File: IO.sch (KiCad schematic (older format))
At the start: 8 parts

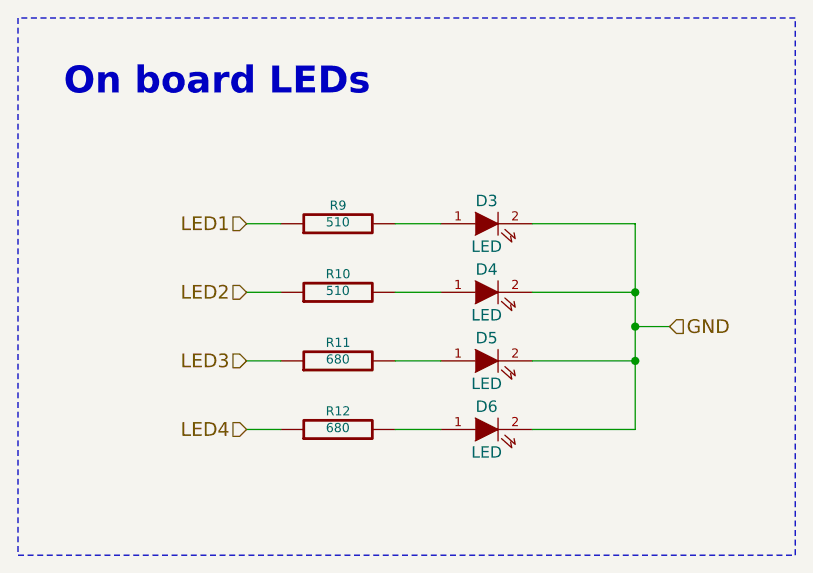
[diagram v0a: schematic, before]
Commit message: - #4 Added UART and CAN interface transceivers - Improved schematic structure - Removed all gerber outputs - Generated schematics outputs for PCB design - Updated local libraries
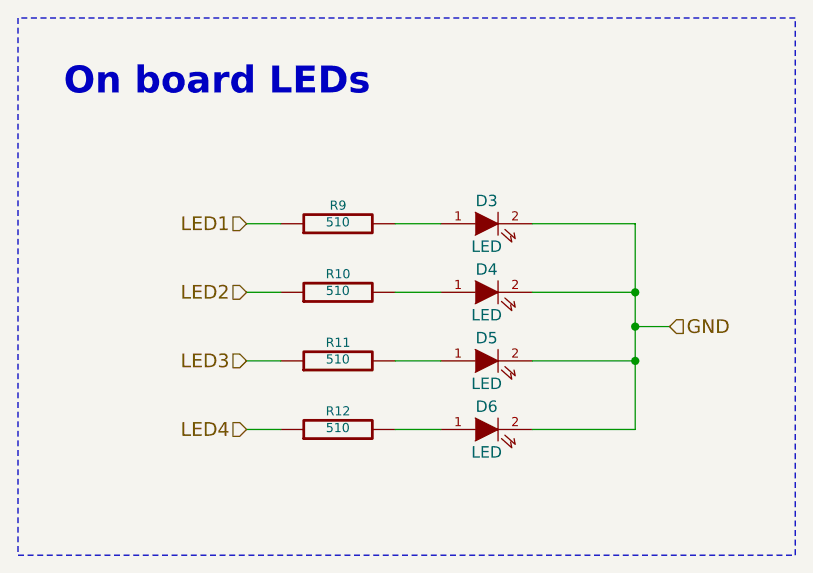
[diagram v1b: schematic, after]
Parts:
- D3, D4, D5, D6: footprint ~ -> LEDs:LED-0805
- R10, R9: footprint ~ -> Resistors_SMD:R_0603_HandSoldering
- R11, R12: value 680 -> 510; footprint ~ -> Resistors_SMD:R_0603_HandSoldering
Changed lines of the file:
@@
 F 0 "D3" H 6300 4150 50  0000 C CNN
 F 1 "LED" H 6300 3950 50  0000 C CNN
-F 2 "~" H 6300 4050 60  0000 C CNN
+F 2 "LEDs:LED-0805" H 6300 4050 60  0001 C CNN
 F 3 "~" H 6300 4050 60  0000 C CNN
 	1    6300 4050
@@
 F 0 "R9" V 5730 4050 40  0000 C CNN
 F 1 "510" V 5657 4051 40  0000 C CNN
-F 2 "~" V 5580 4050 30  0000 C CNN
+F 2 "Resistors_SMD:R_0603_HandSoldering" V 5580 4050 30  0001 C CNN
 F 3 "~" H 5650 4050 30  0000 C CNN
 	1    5650 4050
@@
 F 0 "D4" H 6300 4450 50  0000 C CNN
 F 1 "LED" H 6300 4250 50  0000 C CNN
-F 2 "~" H 6300 4350 60  0000 C CNN
+F 2 "LEDs:LED-0805" H 6300 4350 60  0001 C CNN
 F 3 "~" H 6300 4350 60  0000 C CNN
 	1    6300 4350
@@
 F 0 "R10" V 5730 4350 40  0000 C CNN
 F 1 "510" V 5657 4351 40  0000 C CNN
-F 2 "~" V 5580 4350 30  0000 C CNN
+F 2 "Resistors_SMD:R_0603_HandSoldering" V 5580 4350 30  0001 C CNN
 F 3 "~" H 5650 4350 30  0000 C CNN
 	1    5650 4350
@@
 F 0 "D5" H 6300 4750 50  0000 C CNN
 F 1 "LED" H 6300 4550 50  0000 C CNN
-F 2 "~" H 6300 4650 60  0000 C CNN
+F 2 "LEDs:LED-0805" H 6300 4650 60  0001 C CNN
 F 3 "~" H 6300 4650 60  0000 C CNN
 	1    6300 4650
@@
 P 5650 4650
 F 0 "R11" V 5730 4650 40  0000 C CNN
-F 1 "680" V 5657 4651 40  0000 C CNN
-F 2 "~" V 5580 4650 30  0000 C CNN
+F 1 "510" V 5657 4651 40  0000 C CNN
+F 2 "Resistors_SMD:R_0603_HandSoldering" V 5580 4650 30  0001 C CNN
 F 3 "~" H 5650 4650 30  0000 C CNN
 	1    5650 4650
@@
 F 0 "D6" H 6300 5050 50  0000 C CNN
 F 1 "LED" H 6300 4850 50  0000 C CNN
-F 2 "~" H 6300 4950 60  0000 C CNN
+F 2 "LEDs:LED-0805" H 6300 4950 60  0001 C CNN
 F 3 "~" H 6300 4950 60  0000 C CNN
 	1    6300 4950
@@
 P 5650 4950
 F 0 "R12" V 5730 4950 40  0000 C CNN
-F 1 "680" V 5657 4951 40  0000 C CNN
-F 2 "~" V 5580 4950 30  0000 C CNN
+F 1 "510" V 5657 4951 40  0000 C CNN
+F 2 "Resistors_SMD:R_0603_HandSoldering" V 5580 4950 30  0001 C CNN
 F 3 "~" H 5650 4950 30  0000 C CNN
 	1    5650 4950
